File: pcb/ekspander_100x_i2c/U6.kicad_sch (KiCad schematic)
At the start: 12 parts, among them J15 DG127A-5.08-06P-14-00AH, J16 DG127A-5.08-06P-14-00AH, J17 DG127A-5.08-06P-14-00AH, U30 LTV-847, U31 ITS716G, U32 ITS716G, U33 LTV-847, U6 MCP23017_SP

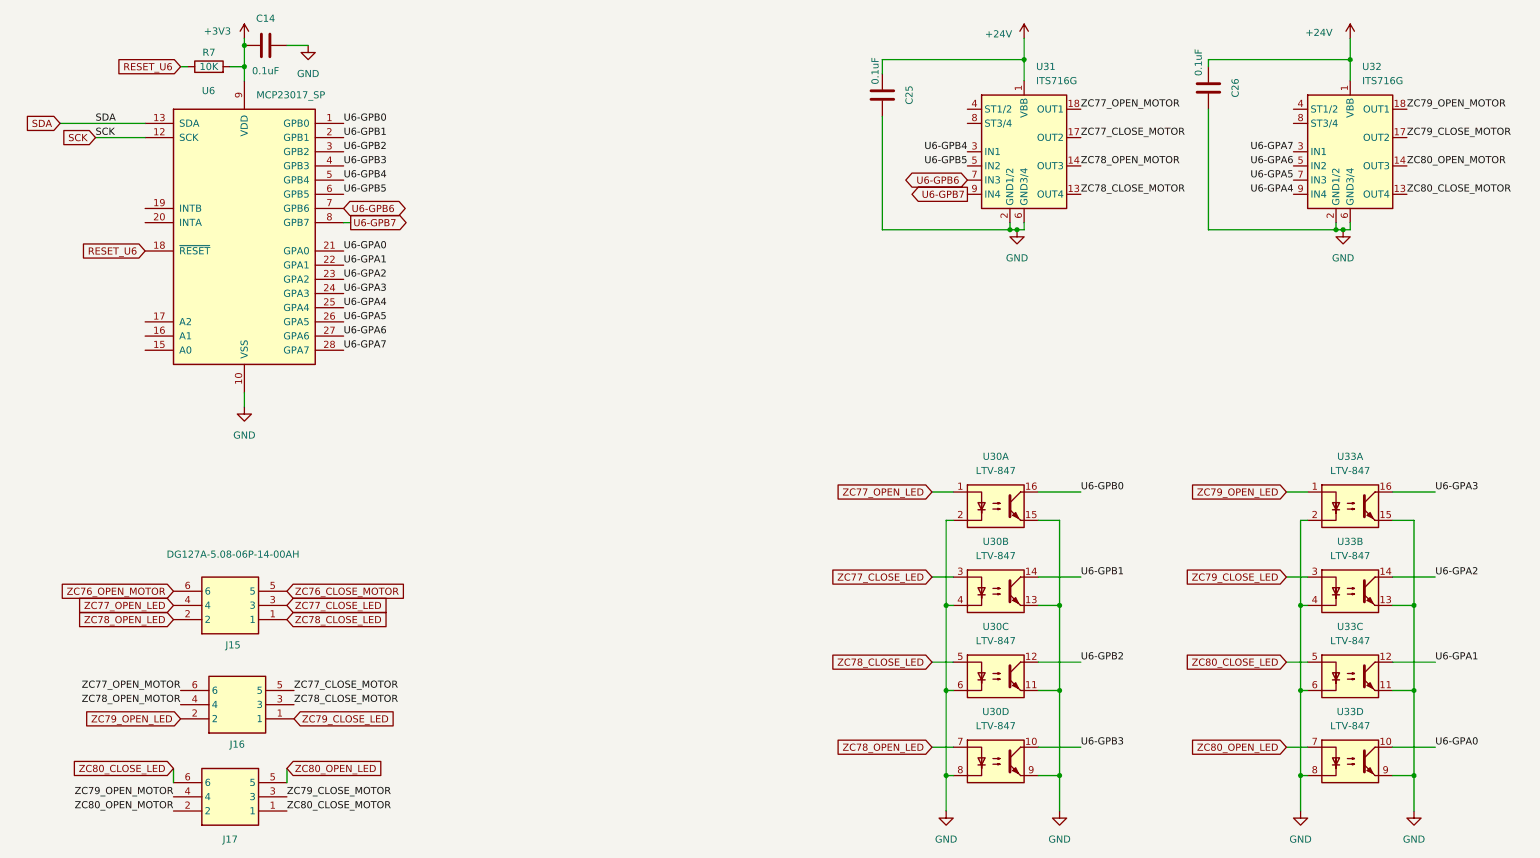
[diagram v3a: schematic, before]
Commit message: Ekspander 100x - finish J
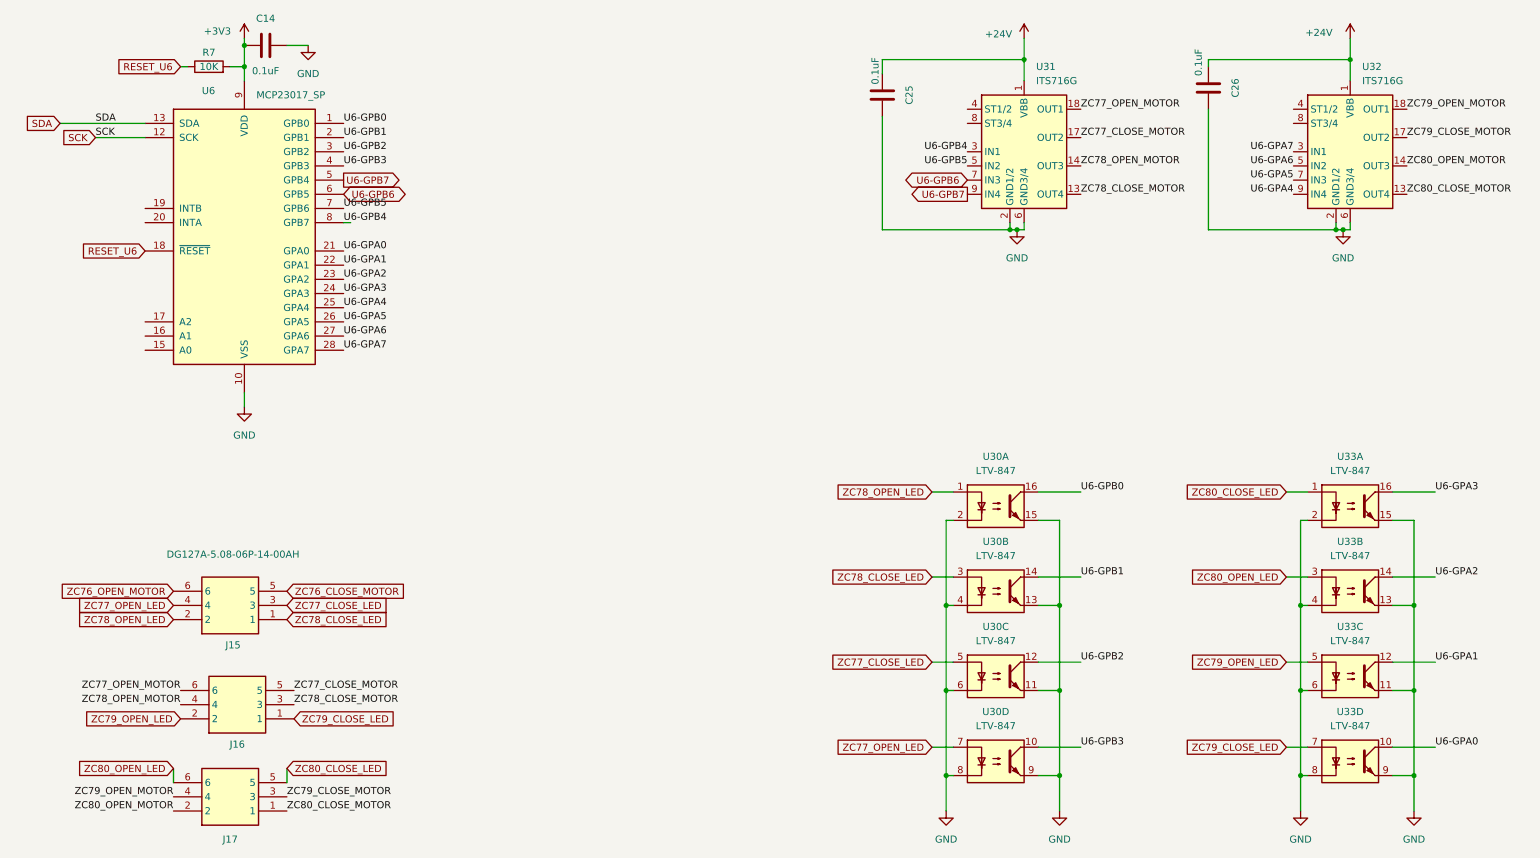
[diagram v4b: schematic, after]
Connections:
- net U6-GPB4: now also U6.8 (GPB7); no longer U6.5 (GPB4)
- net U6-GPB5: now also U6.7 (GPB6); no longer U6.6 (GPB5)
- net U6-GPB6: now also U6.6 (GPB5); no longer U6.7 (GPB6)
- net U6-GPB7: now also U6.5 (GPB4); no longer U6.8 (GPB7)
- net ZC77_CLOSE_LED: now also U30.5; no longer U30.3
- net ZC77_OPEN_LED: now also U30.7; no longer U30.1
- net ZC78_CLOSE_LED: now also U30.3; no longer U30.5
- net ZC78_OPEN_LED: now also U30.1; no longer U30.7
- net ZC79_CLOSE_LED: now also U33.7; no longer U33.3
- net ZC79_OPEN_LED: now also U33.5; no longer U33.1
- net ZC80_CLOSE_LED: now also J17.5, U33.1; no longer J17.6, U33.5
- net ZC80_OPEN_LED: now also J17.6, U33.3; no longer J17.5, U33.7
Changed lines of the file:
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@@
 	)
 	(label "U6-GPB5"
-		(at 72.39 45.72 0)
-		(effects
-			(font
-				(size 1.27 1.27)
-			)
-			(justify left bottom)
-		)
-		(property "Netclass" "GPIO"
-			(at 82.296 45.72 0)
+		(at 72.39 48.26 0)
+		(effects
+			(font
+				(size 1.27 1.27)
+			)
+			(justify left bottom)
+		)
+		(property "Netclass" "GPIO"
+			(at 82.296 48.26 0)
 			(effects
 				(font
@@
 	)
 	(label "U6-GPB4"
-		(at 72.39 43.18 0)
-		(effects
-			(font
-				(size 1.27 1.27)
-			)
-			(justify left bottom)
-		)
-		(property "Netclass" "GPIO"
-			(at 82.55 43.18 0)
+		(at 72.39 50.8 0)
+		(effects
+			(font
+				(size 1.27 1.27)
+			)
+			(justify left bottom)
+		)
+		(property "Netclass" "GPIO"
+			(at 82.55 50.8 0)
 			(effects
 				(font
@@
 	(global_label "U6-GPB7"
 		(shape output)
-		(at 73.66 50.8 0)
+		(at 72.39 43.18 0)
 		(fields_autoplaced yes)
 		(effects
@@
 		)
 		(property "Intersheetrefs" "${INTERSHEET_REFS}"
-			(at 85.7771 50.8 0)
+			(at 84.5071 43.18 0)
 			(effects
 				(font
@@
 	(global_label "ZC77_OPEN_LED"
 		(shape input)
-		(at 177.8 99.06 180)
-		(fields_autoplaced yes)
-		(effects
-			(font
-				(size 1.27 1.27)
-			)
-			(justify right)
-		)
-		(property "Intersheetrefs" "${INTERSHEET_REFS}"
-			(at 159.454 99.06 0)
+		(at 177.8 144.78 180)
+		(fields_autoplaced yes)
+		(effects
+			(font
+				(size 1.27 1.27)
+			)
+			(justify right)
+		)
+		(property "Intersheetrefs" "${INTERSHEET_REFS}"
+			(at 159.454 144.78 0)
 			(effects
 				(font
@@
 	(global_label "ZC80_CLOSE_LED"
 		(shape input)
-		(at 41.91 148.59 180)
-		(fields_autoplaced yes)
-		(effects
-			(font
-				(size 1.27 1.27)
-			)
-			(justify right)
-		)
-		(property "Intersheetrefs" "${INTERSHEET_REFS}"
-			(at 22.6569 148.59 0)
-			(effects
-				(font
-					(size 1.27 1.27)
-				)
-				(justify right)
+		(at 62.23 148.59 0)
+		(fields_autoplaced yes)
+		(effects
+			(font
+				(size 1.27 1.27)
+			)
+			(justify left)
+		)
+		(property "Intersheetrefs" "${INTERSHEET_REFS}"
+			(at 80.576 148.59 0)
+			(effects
+				(font
+					(size 1.27 1.27)
+				)
+				(justify left)
 				(hide yes)
 			)
@@
 	(global_label "ZC78_CLOSE_LED"
 		(shape input)
-		(at 177.8 129.54 180)
-		(fields_autoplaced yes)
-		(effects
-			(font
-				(size 1.27 1.27)
-			)
-			(justify right)
-		)
-		(property "Intersheetrefs" "${INTERSHEET_REFS}"
-			(at 158.5469 129.54 0)
+		(at 177.8 114.3 180)
+		(fields_autoplaced yes)
+		(effects
+			(font
+				(size 1.27 1.27)
+			)
+			(justify right)
+		)
+		(property "Intersheetrefs" "${INTERSHEET_REFS}"
+			(at 158.5469 114.3 0)
 			(effects
 				(font
@@
 	(global_label "ZC80_CLOSE_LED"
 		(shape input)
-		(at 241.3 129.54 180)
-		(fields_autoplaced yes)
-		(effects
-			(font
-				(size 1.27 1.27)
-			)
-			(justify right)
-		)
-		(property "Intersheetrefs" "${INTERSHEET_REFS}"
-			(at 222.0469 129.54 0)
+		(at 241.3 99.06 180)
+		(fields_autoplaced yes)
+		(effects
+			(font
+				(size 1.27 1.27)
+			)
+			(justify right)
+		)
+		(property "Intersheetrefs" "${INTERSHEET_REFS}"
+			(at 222.954 99.06 0)
 			(effects
 				(font
@@
 	(global_label "ZC79_OPEN_LED"
 		(shape input)
-		(at 241.3 99.06 180)
-		(fields_autoplaced yes)
-		(effects
-			(font
-				(size 1.27 1.27)
-			)
-			(justify right)
-		)
-		(property "Intersheetrefs" "${INTERSHEET_REFS}"
-			(at 222.954 99.06 0)
+		(at 241.3 129.54 180)
+		(fields_autoplaced yes)
+		(effects
+			(font
+				(size 1.27 1.27)
+			)
+			(justify right)
+		)
+		(property "Intersheetrefs" "${INTERSHEET_REFS}"
+			(at 222.0469 129.54 0)
 			(effects
 				(font
@@
 	(global_label "ZC80_OPEN_LED"
 		(shape input)
+		(at 241.3 114.3 180)
+		(fields_autoplaced yes)
+		(effects
+			(font
+				(size 1.27 1.27)
+			)
+			(justify right)
+		)
+		(property "Intersheetrefs" "${INTERSHEET_REFS}"
+			(at 222.0469 114.3 0)
+			(effects
+				(font
+					(size 1.27 1.27)
+				)
+				(justify right)
+				(hide yes)
+			)
+		)
+	)
+	(global_label "ZC79_CLOSE_LED"
+		(shape input)
+		(at 63.5 139.7 0)
+		(fields_autoplaced yes)
+		(effects
+			(font
+				(size 1.27 1.27)
+			)
+			(justify left)
+		)
+		(property "Intersheetrefs" "${INTERSHEET_REFS}"
+			(at 82.7531 139.7 0)
+			(effects
+				(font
+					(size 1.27 1.27)
+				)
+				(justify left)
+				(hide yes)
+			)
+		)
+	)
+	(global_label "ZC79_CLOSE_LED"
+		(shape input)
 		(at 241.3 144.78 180)
 		(fields_autoplaced yes)
@@
 		)
 	)
-	(global_label "ZC79_CLOSE_LED"
-		(shape input)
-		(at 63.5 139.7 0)
-		(fields_autoplaced yes)
-		(effects
-			(font
-				(size 1.27 1.27)
-			)
-			(justify left)
-		)
-		(property "Intersheetrefs" "${INTERSHEET_REFS}"
-			(at 82.7531 139.7 0)
-			(effects
-				(font
-					(size 1.27 1.27)
-				)
-				(justify left)
-				(hide yes)
-			)
-		)
-	)
-	(global_label "ZC79_CLOSE_LED"
-		(shape input)
-		(at 241.3 114.3 180)
-		(fields_autoplaced yes)
-		(effects
-			(font
-				(size 1.27 1.27)
-			)
-			(justify right)
-		)
-		(property "Intersheetrefs" "${INTERSHEET_REFS}"
-			(at 222.0469 114.3 0)
-			(effects
-				(font
-					(size 1.27 1.27)
-				)
-				(justify right)
-				(hide yes)
-			)
-		)
-	)
 	(global_label "ZC76_OPEN_MOTOR"
 		(shape input)
@@
 	(global_label "ZC77_CLOSE_LED"
 		(shape input)
-		(at 177.8 114.3 180)
-		(fields_autoplaced yes)
-		(effects
-			(font
-				(size 1.27 1.27)
-			)
-			(justify right)
-		)
-		(property "Intersheetrefs" "${INTERSHEET_REFS}"
-			(at 158.5469 114.3 0)
+		(at 177.8 129.54 180)
+		(fields_autoplaced yes)
+		(effects
+			(font
+				(size 1.27 1.27)
+			)
+			(justify right)
+		)
+		(property "Intersheetrefs" "${INTERSHEET_REFS}"
+			(at 158.5469 129.54 0)
 			(effects
 				(font
@@
 	(global_label "U6-GPB6"
 		(shape bidirectional)
-		(at 72.39 48.26 0)
+		(at 72.39 45.72 0)
 		(fields_autoplaced yes)
 		(effects
@@
 		)
 		(property "Intersheetrefs" "${INTERSHEET_REFS}"
-			(at 85.6184 48.26 0)
+			(at 85.6184 45.72 0)
 			(effects
 				(font
@@
 	(global_label "ZC80_OPEN_LED"
 		(shape input)
-		(at 62.23 148.59 0)
-		(fields_autoplaced yes)
-		(effects
-			(font
-				(size 1.27 1.27)
-			)
-			(justify left)
-		)
-		(property "Intersheetrefs" "${INTERSHEET_REFS}"
-			(at 80.576 148.59 0)
-			(effects
-				(font
-					(size 1.27 1.27)
-				)
-				(justify left)
+		(at 41.91 148.59 180)
+		(fields_autoplaced yes)
+		(effects
+			(font
+				(size 1.27 1.27)
+			)
+			(justify right)
+		)
+		(property "Intersheetrefs" "${INTERSHEET_REFS}"
+			(at 22.6569 148.59 0)
+			(effects
+				(font
+					(size 1.27 1.27)
+				)
+				(justify right)
 				(hide yes)
 			)
@@
 	(global_label "ZC78_OPEN_LED"
 		(shape input)
-		(at 177.8 144.78 180)
-		(fields_autoplaced yes)
-		(effects
-			(font
-				(size 1.27 1.27)
-			)
-			(justify right)
-		)
-		(property "Intersheetrefs" "${INTERSHEET_REFS}"
-			(at 159.454 144.78 0)
-			(effects
-				(font
+		(at 177.8 99.06 180)
+		(fields_autoplaced yes)
+		(effects
+			(font
+				(size 1.27 1.27)
+			)
+			(justify right)
+		)
+		(property "Intersheetrefs" "${INTERSHEET_REFS}"
+			(at 159.454 99.06 0)
+			(effects
+				(font

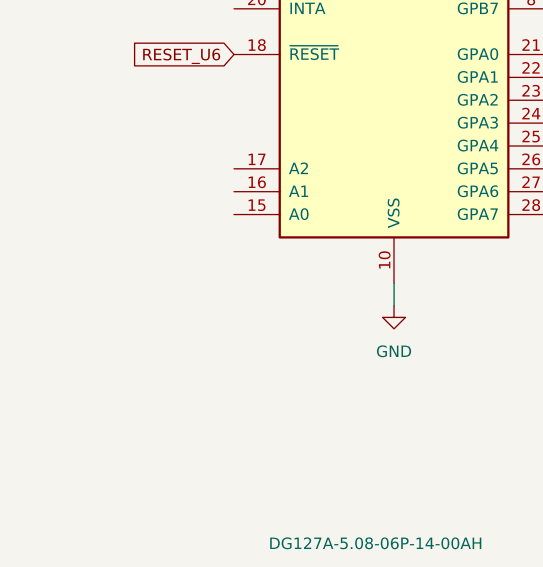
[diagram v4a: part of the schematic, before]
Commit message: Ekspander 100x - adresacja I2C - MCP23017
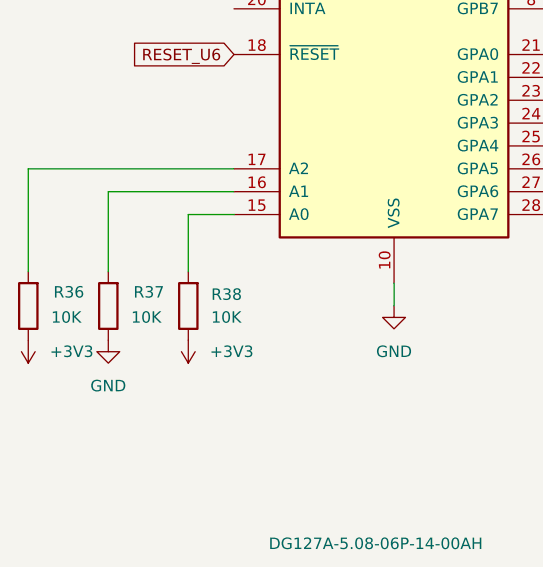
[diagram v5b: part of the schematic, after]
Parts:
- added R36, R37, R38: 10K, PCM_Resistor_SMD_AKL:R_0805_2012Metric_Pad1.20x1.40mm_HandSolder, symbol Device:R
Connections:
- net +3V3: now also R36.1, R38.1
- net GND: now also R37.1
- net at U6.15 (A0): now also R38.2
- net at U6.16 (A1): now also R37.2
- net at U6.17 (A2): now also R36.2

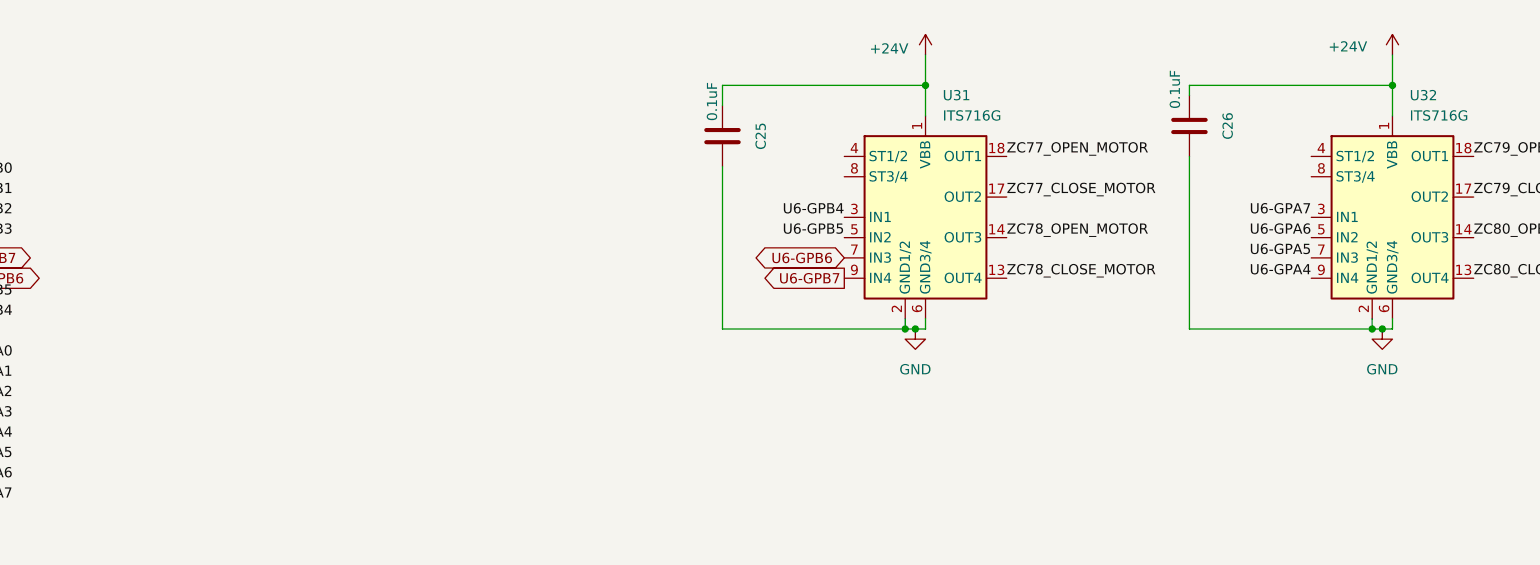
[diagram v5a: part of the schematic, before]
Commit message: Ekspander 100x - diagnostic LEDs
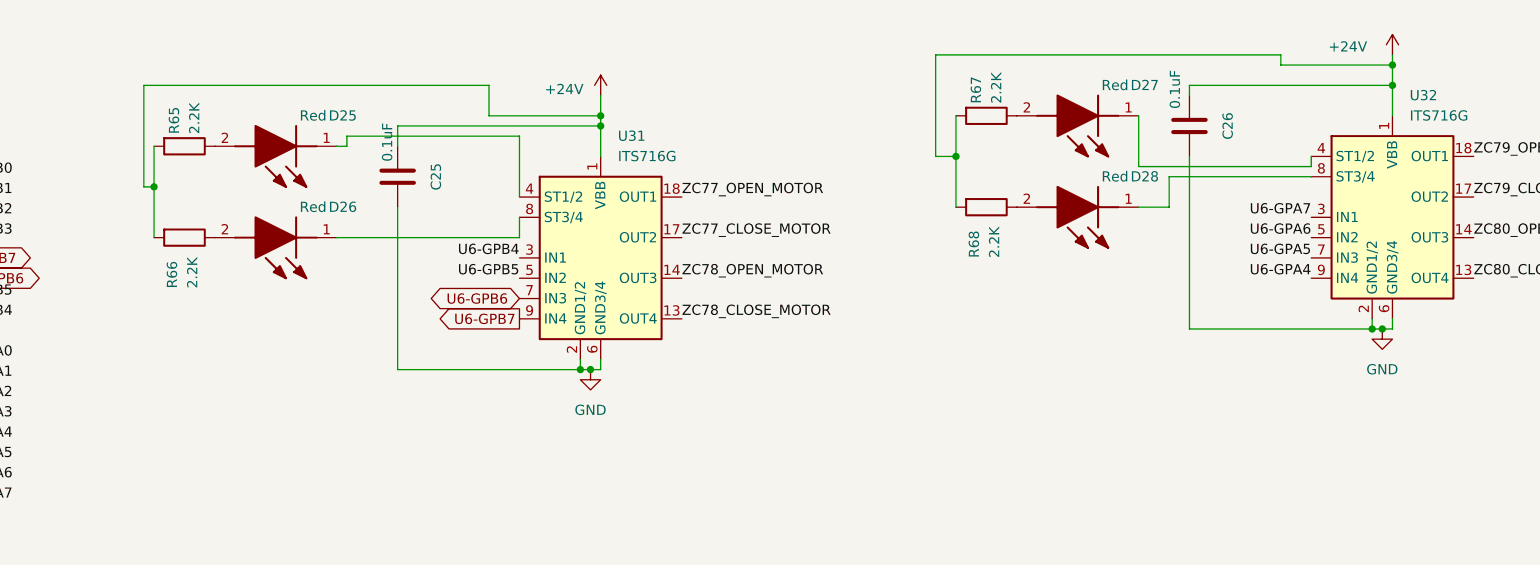
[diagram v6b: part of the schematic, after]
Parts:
- added D25, D26, D27, D28: Red, 1_tme:LEDC2012X120N, symbol LTST-C170KRKT:LTST-C170KRKT
- added R65, R66, R67, R68: 2.2K, PCM_Resistor_SMD_AKL:R_0805_2012Metric_Pad1.20x1.40mm_HandSolder, symbol Device:R
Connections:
- net +24V: now also R65.2, R66.2, R67.2, R68.2
- net at U32.4 (ST1/2): now also D27.1 (K)
- net at U32.8 (ST3/4): now also D28.1 (K)
- net at U31.4 (ST1/2): now also D25.1 (K)
- net at U31.8 (ST3/4): now also D26.1 (K)
- new net: D25.2 (A), R65.1
- new net: D28.2 (A), R68.1
- new net: D27.2 (A), R67.1
- new net: D26.2 (A), R66.1
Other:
- moved on the sheet: C25, U31
